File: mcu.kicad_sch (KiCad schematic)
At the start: 65 parts, among them J1 USB_C, P20 HEADER-2x11, P22 HEADER-2x13, P26 LPC_JTAG, P28 HEADER-2x11, SW1 SWITCH, SW2 SWITCH, U15 TVS_USB, U20 W25Q80, U23 LPC4330FET180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

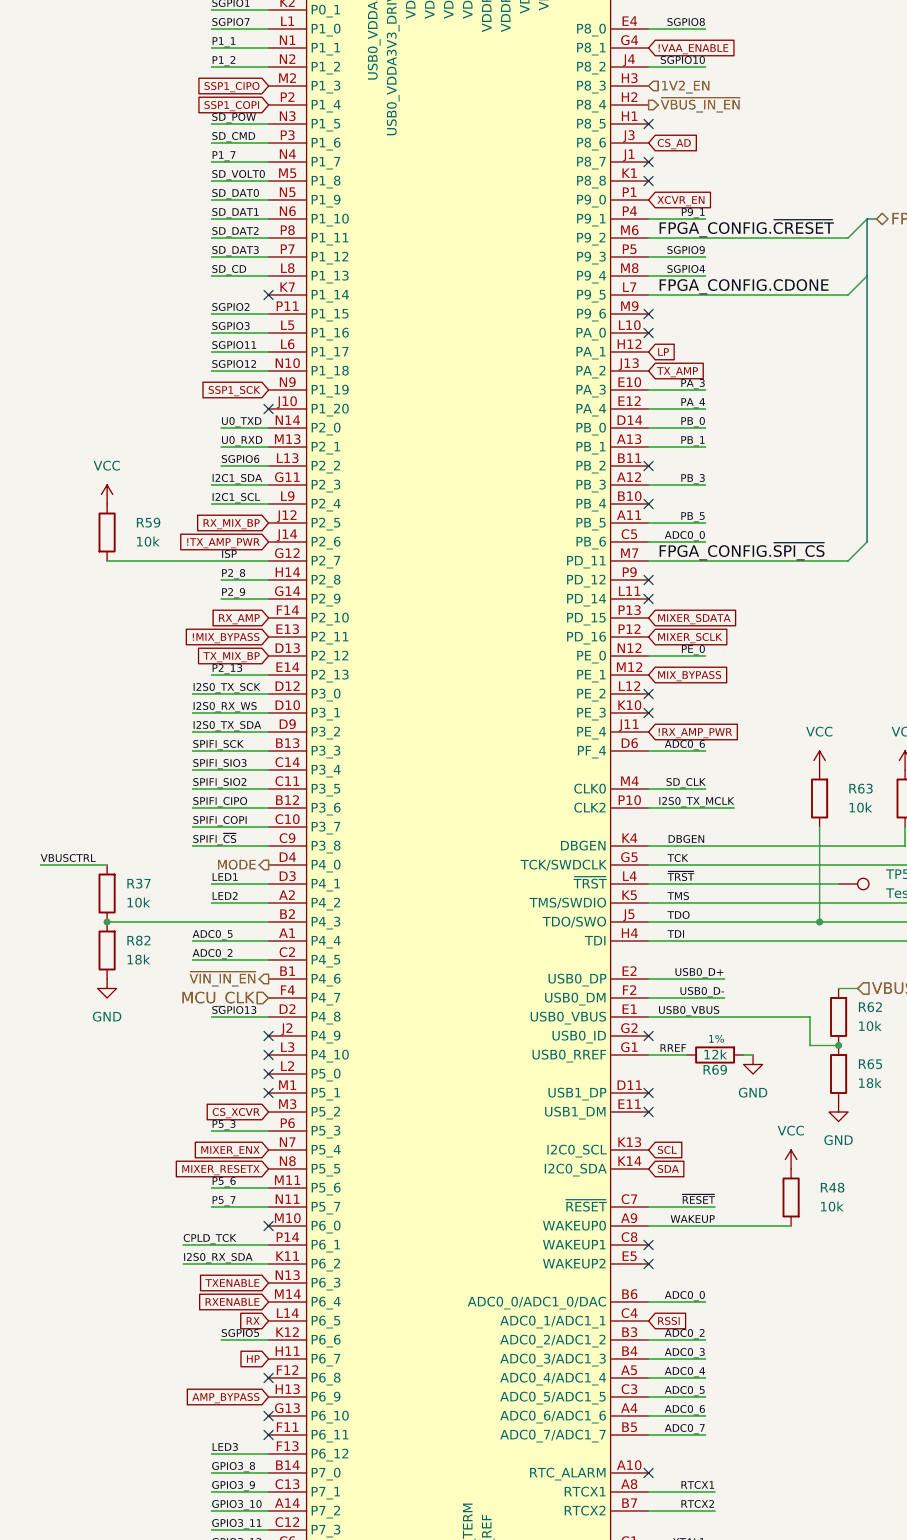
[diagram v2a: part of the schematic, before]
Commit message: Rearrange RF section
- Use DPDT RF switches to reduce long tracks
- Add limiter
- Add switch control logic
- Move ADC/DAC U18 to RF area
- Remove baseband header P9
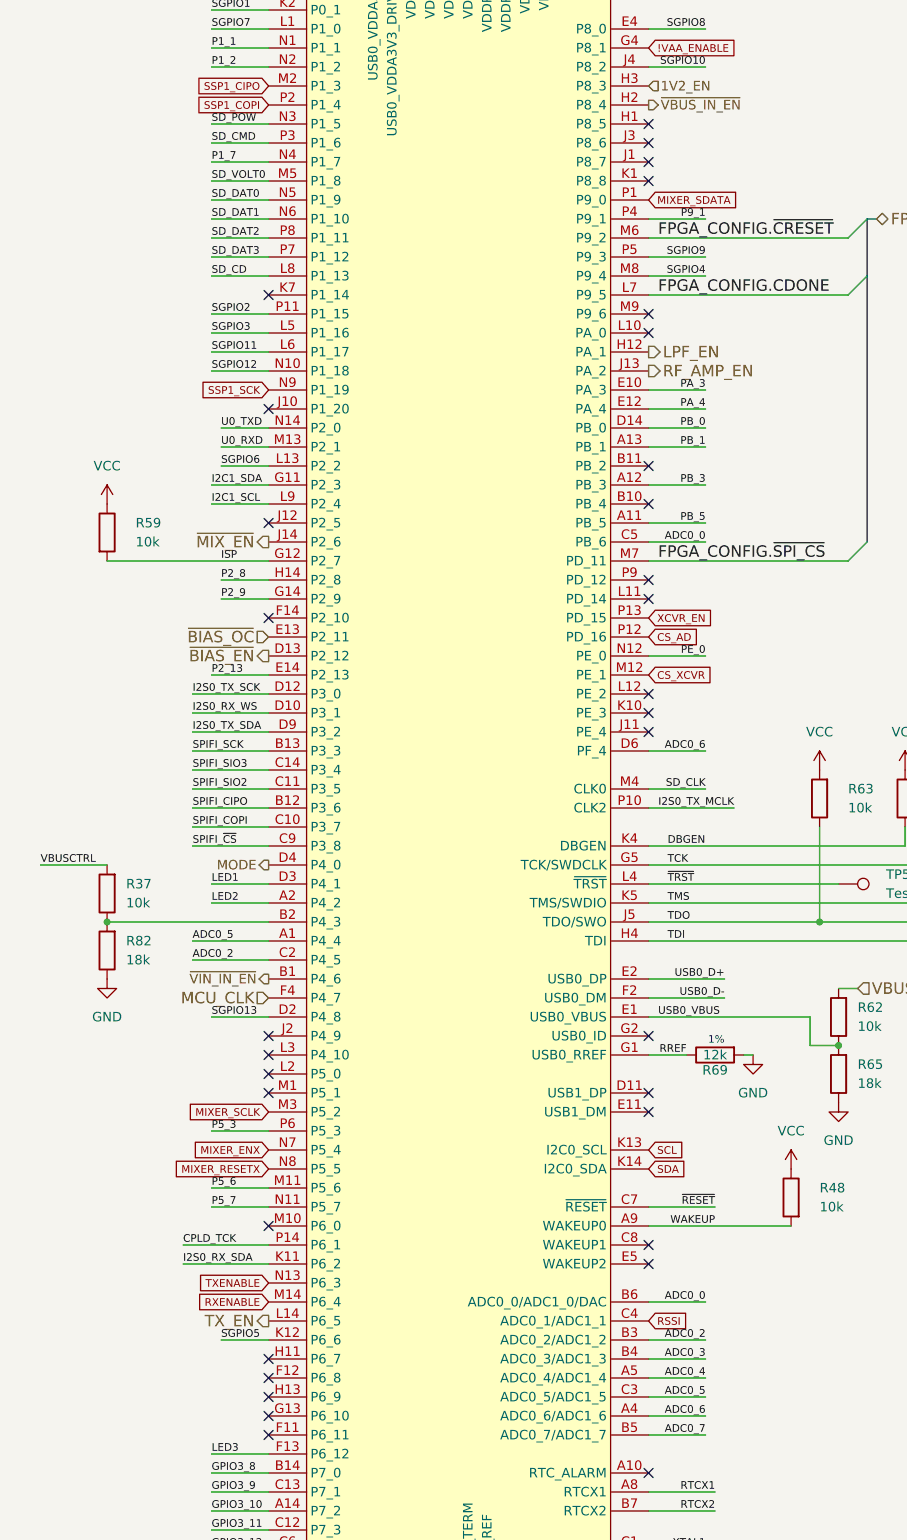
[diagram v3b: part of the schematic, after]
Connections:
- net MIX_BYPASS is gone; now on net CS_XCVR: U23.M12 (PE_1)
- net CS_AD: now also U23.P12 (PD_16); no longer U23.J3 (P8_6)
- net CS_XCVR: no longer U23.M3 (P5_2)
- net MIXER_SCLK: now also U23.M3 (P5_2); no longer U23.P12 (PD_16)
- net MIXER_SDATA: now also U23.P1 (P9_0); no longer U23.P13 (PD_15)
- net XCVR_EN: now also U23.P13 (PD_15); no longer U23.P1 (P9_0)
- net !MIX_BYPASS renamed ~{BIAS_OC}
- net !RX_AMP_PWR: no longer names the net of U23.J11 (PE_4)
- net !TX_AMP_PWR renamed ~{MIX_EN}
- net AMP_BYPASS: no longer names the net of U23.H13 (P6_9)
- net HP: no longer names the net of U23.H11 (P6_7)
- net LP renamed LPF_EN
- net RX renamed TX_EN
- net RX_AMP: no longer names the net of U23.F14 (P2_10)
- net RX_MIX_BP: no longer names the net of U23.J12 (P2_5)
- net TX_AMP renamed RF_AMP_EN
- net TX_MIX_BP renamed ~{BIAS_EN}
- no-connect marks 31 -> 37
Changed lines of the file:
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@@
 	)
 	(no_connect
+		(at 194.31 218.44)
+	)
+	(no_connect
 		(at 245.11 175.26)
 	)
@@
 	)
 	(no_connect
+		(at 245.11 134.62)
+	)
+	(no_connect
 		(at 194.31 175.26)
 	)
 	(no_connect
+		(at 245.11 55.88)
+	)
+	(no_connect
 		(at 41.91 97.79)
 	)
@@
 	)
 	(no_connect
+		(at 194.31 223.52)
+	)
+	(no_connect
 		(at 245.11 251.46)
 	)
@@
 	)
 	(no_connect
+		(at 194.31 119.38)
+	)
+	(no_connect
 		(at 245.11 182.88)
 	)
@@
 	)
 	(no_connect
+		(at 194.31 106.68)
+	)
+	(no_connect
 		(at 245.11 60.96)
 	)
@@
 		)
 	)
-	(global_label "!RX_AMP_PWR"
-		(shape input)
-		(at 245.11 134.62 0)
-		(fields_autoplaced yes)
-		(effects
-			(font
-				(size 1.016 1.016)
-			)
-			(justify left)
-		)
-		(property "Intersheetrefs" "${INTERSHEET_REFS}"
-			(at 257.2314 134.62 0)
-			(effects
-				(font
-					(size 1.27 1.27)
-				)
-				(justify left)
-				(hide yes)
-			)
-		)
-	)
-	(global_label "RX_MIX_BP"
-		(shape input)
-		(at 194.31 106.68 180)
-		(fields_autoplaced yes)
-		(effects
-			(font
-				(size 1.016 1.016)
-			)
-			(justify right)
-		)
-		(property "Intersheetrefs" "${INTERSHEET_REFS}"
-			(at 184.269 106.68 0)
-			(effects
-				(font
-					(size 1.27 1.27)
-				)
-				(justify right)
-				(hide yes)
-			)
-		)
-	)
 	(global_label "XCVR_EN"
 		(shape input)
-		(at 245.11 63.5 0)
-		(fields_autoplaced yes)
-		(effects
-			(font
-				(size 1.016 1.016)
-			)
-			(justify left)
-		)
-		(property "Intersheetrefs" "${INTERSHEET_REFS}"
-			(at 253.6029 63.5 0)
-			(effects
-				(font
-					(size 1.27 1.27)
-				)
-				(justify left)
-				(hide yes)
-			)
-		)
-	)
-	(global_label "LP"
-		(shape input)
-		(at 245.11 83.82 0)
+		(at 245.11 119.38 0)
 		(fields_autoplaced yes)
 		(effects
@@
 		)
 		(property "Intersheetrefs" "${INTERSHEET_REFS}"
-			(at 248.8132 83.82 0)
+			(at 253.6029 119.38 0)
 			(effects
 				(font
@@
 		)
 	)
-	(global_label "TX_MIX_BP"
-		(shape input)
-		(at 194.31 124.46 180)
-		(fields_autoplaced yes)
-		(effects
-			(font
-				(size 1.016 1.016)
-			)
-			(justify right)
-		)
-		(property "Intersheetrefs" "${INTERSHEET_REFS}"
-			(at 184.5109 124.46 0)
-			(effects
-				(font
-					(size 1.27 1.27)
-				)
-				(justify right)
-				(hide yes)
-			)
-		)
-	)
 	(global_label "MIXER_SCLK"
 		(shape input)
-		(at 245.11 121.92 0)
-		(fields_autoplaced yes)
-		(effects
-			(font
-				(size 1.016 1.016)
-			)
-			(justify left)
-		)
-		(property "Intersheetrefs" "${INTERSHEET_REFS}"
-			(at 256.1186 121.92 0)
-			(effects
-				(font
-					(size 1.27 1.27)
-				)
-				(justify left)
-				(hide yes)
-			)
-		)
-	)
-	(global_label "RX_AMP"
-		(shape input)
-		(at 194.31 119.38 180)
+		(at 194.31 185.42 180)
 		(fields_autoplaced yes)
 		(effects
@@
 		)
 		(property "Intersheetrefs" "${INTERSHEET_REFS}"
-			(at 186.6396 119.38 0)
+			(at 183.3014 185.42 0)
 			(effects
 				(font
@@
 	(global_label "CS_XCVR"
 		(shape input)
-		(at 194.31 185.42 180)
-		(fields_autoplaced yes)
-		(effects
-			(font
-				(size 1.016 1.016)
-			)
-			(justify right)
-		)
-		(property "Intersheetrefs" "${INTERSHEET_REFS}"
-			(at 185.8171 185.42 0)
-			(effects
-				(font
-					(size 1.27 1.27)
-				)
-				(justify right)
-				(hide yes)
-			)
-		)
-	)
-	(global_label "RX"
-		(shape input)
-		(at 194.31 213.36 180)
+		(at 245.11 127 0)
 		(fields_autoplaced yes)
 		(effects
@@
 				(size 1.016 1.016)
 			)
-			(justify right)
+			(justify left)
 		)
 		(property "Intersheetrefs" "${INTERSHEET_REFS}"
-			(at 190.4617 213.36 0)
+			(at 253.6029 127 0)
 			(effects
 				(font
 					(size 1.27 1.27)
 				)
-				(justify right)
+				(justify left)
 				(hide yes)
 			)
@@
 		)
 	)
-	(global_label "!TX_AMP_PWR"
-		(shape input)
-		(at 194.31 109.22 180)
-		(fields_autoplaced yes)
-		(effects
-			(font
-				(size 1.016 1.016)
-			)
-			(justify right)
-		)
-		(property "Intersheetrefs" "${INTERSHEET_REFS}"
-			(at 182.4305 109.22 0)
-			(effects
-				(font
-					(size 1.27 1.27)
-				)
-				(justify right)
-				(hide yes)
-			)
-		)
-	)
 	(global_label "RXENABLE"
 		(shape input)
@@
 		)
 	)
-	(global_label "TX_AMP"
-		(shape input)
-		(at 245.11 86.36 0)
-		(fields_autoplaced yes)
-		(effects
-			(font
-				(size 1.016 1.016)
-			)
-			(justify left)
-		)
-		(property "Intersheetrefs" "${INTERSHEET_REFS}"
-			(at 252.5385 86.36 0)
-			(effects
-				(font
-					(size 1.27 1.27)
-				)
-				(justify left)
-				(hide yes)
-			)
-		)
-	)
-	(global_label "MIX_BYPASS"
-		(shape input)
-		(at 245.11 127 0)
-		(fields_autoplaced yes)
-		(effects
-			(font
-				(size 1.016 1.016)
-			)
-			(justify left)
-		)
-		(property "Intersheetrefs" "${INTERSHEET_REFS}"
-			(at 256.0703 127 0)
-			(effects
-				(font
-					(size 1.27 1.27)
-				)
-				(justify left)
-				(hide yes)
-			)
-		)
-	)
 	(global_label "TXENABLE"
 		(shape input)
@@
 		)
 	)
-	(global_label "HP"
-		(shape input)
-		(at 194.31 218.44 180)
-		(fields_autoplaced yes)
-		(effects
-			(font
-				(size 1.016 1.016)
-			)
-			(justify right)
-		)
-		(property "Intersheetrefs" "${INTERSHEET_REFS}"
-			(at 190.3649 218.44 0)
-			(effects
-				(font
-					(size 1.27 1.27)
-				)
-				(justify right)
-				(hide yes)
-			)
-		)
-	)
-	(global_label "!MIX_BYPASS"
-		(shape input)
-		(at 194.31 121.92 180)
-		(fields_autoplaced yes)
-		(effects
-			(font
-				(size 1.016 1.016)
-			)
-			(justify right)
-		)
-		(property "Intersheetrefs" "${INTERSHEET_REFS}"
-			(at 182.8659 121.92 0)
-			(effects
-				(font
-					(size 1.27 1.27)
-				)
-				(justify right)
-				(hide yes)
-			)
-		)
-	)
 	(global_label "MIXER_RESETX"
 		(shape input)
@@
 	(global_label "MIXER_SDATA"
 		(shape input)
-		(at 245.11 119.38 0)
+		(at 245.11 63.5 0)
 		(fields_autoplaced yes)
 		(effects
@@
 		)
 		(property "Intersheetrefs" "${INTERSHEET_REFS}"
-			(at 256.796 119.38 0)
+			(at 256.796 63.5 0)
 			(effects
 				(font
@@
 		)
 	)
-	(global_label "AMP_BYPASS"
-		(shape input)
-		(at 194.31 223.52 180)
-		(fields_autoplaced yes)
-		(effects
-			(font
-				(size 1.016 1.016)
-			)
-			(justify right)
-		)
-		(property "Intersheetrefs" "${INTERSHEET_REFS}"
-			(at 182.9142 223.52 0)
-			(effects
-				(font
-					(size 1.27 1.27)
-				)
-				(justify right)
-				(hide yes)
-			)
-		)
-	)
 	(global_label "CS_AD"
 		(shape input)
-		(at 245.11 55.88 0)
+		(at 245.11 121.92 0)
 		(fields_autoplaced yes)
 		(effects
@@
 		)
 		(property "Intersheetrefs" "${INTERSHEET_REFS}"
-			(at 251.6193 55.88 0)
+			(at 251.6193 121.92 0)
 			(effects
 				(font
@@
 		)
 	)
+	(hierarchical_label "~{BIAS_OC}"
+		(shape input)
+		(at 194.31 121.92 180)
+		(fields_autoplaced yes)
+		(effects
+			(font
+				(size 1.524 1.524)
+			)
+			(justify right)
+		)
+	)
+	(hierarchical_label "LPF_EN"
+		(shape output)
+		(at 245.11 83.82 0)
+		(fields_autoplaced yes)
+		(effects
+			(font
+				(size 1.524 1.524)
+			)
+			(justify left)
+		)
+	)
 	(hierarchical_label "CLKOUT"
 		(shape input)
@@
 		)
 	)
+	(hierarchical_label "~{MIX_EN}"
+		(shape output)
+		(at 194.31 109.22 180)
+		(fields_autoplaced yes)
+		(effects
+			(font
+				(size 1.524 1.524)
+			)
+			(justify right)
+		)
+	)
 	(hierarchical_label "1V2_EN"
 		(shape input)
@@
 			)
 			(justify right)
+		)
+	)
+	(hierarchical_label "RF_AMP_EN"
+		(shape output)
+		(at 245.11 86.36 0)
+		(fields_autoplaced yes)
+		(effects
+			(font
+				(size 1.524 1.524)
+			)
+			(justify left)
+		)
+	)
+	(hierarchical_label "TX_EN"
+		(shape output)
+		(at 194.31 213.36 180)
+		(fields_autoplaced yes)
+		(effects
+			(font
+				(size 1.524 1.524)
+			)
+			(justify right)
+		)
+	)
+	(hierarchical_label "~{BIAS_EN}"
+		(shape output)
+		(at 194.31 124.46 180)
+		(fields_autoplaced yes)
+		(effects
+			(font
+				(size 1.524 1.524)
+			)
+			(justify right)
